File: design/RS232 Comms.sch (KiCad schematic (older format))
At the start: 9 parts, among them J1 JACK_2P, K3 jumper, K4 jumper, U7 MAX232

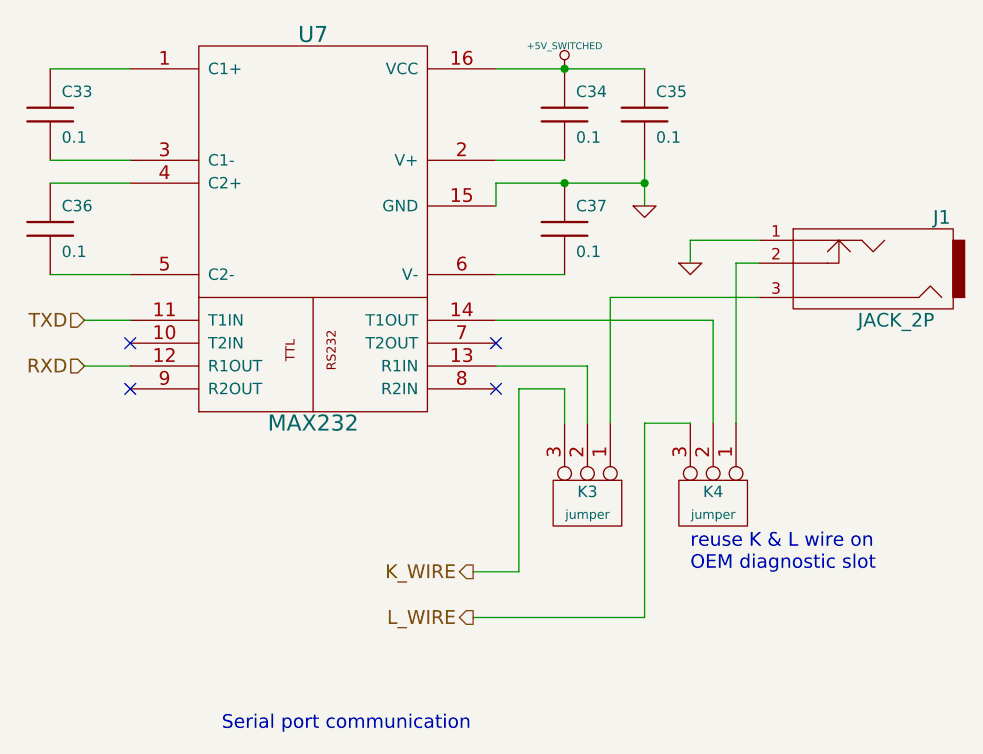
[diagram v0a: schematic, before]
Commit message: revise schema according to Jaguar & Ravage project, eliminate as many errors as possible which were inherited from Puma board. Remove VSS interface, narrow band O2 interface, AC relay output, AC signal input. Make fuel injection configurable which can be batch fired or semi sequential fired
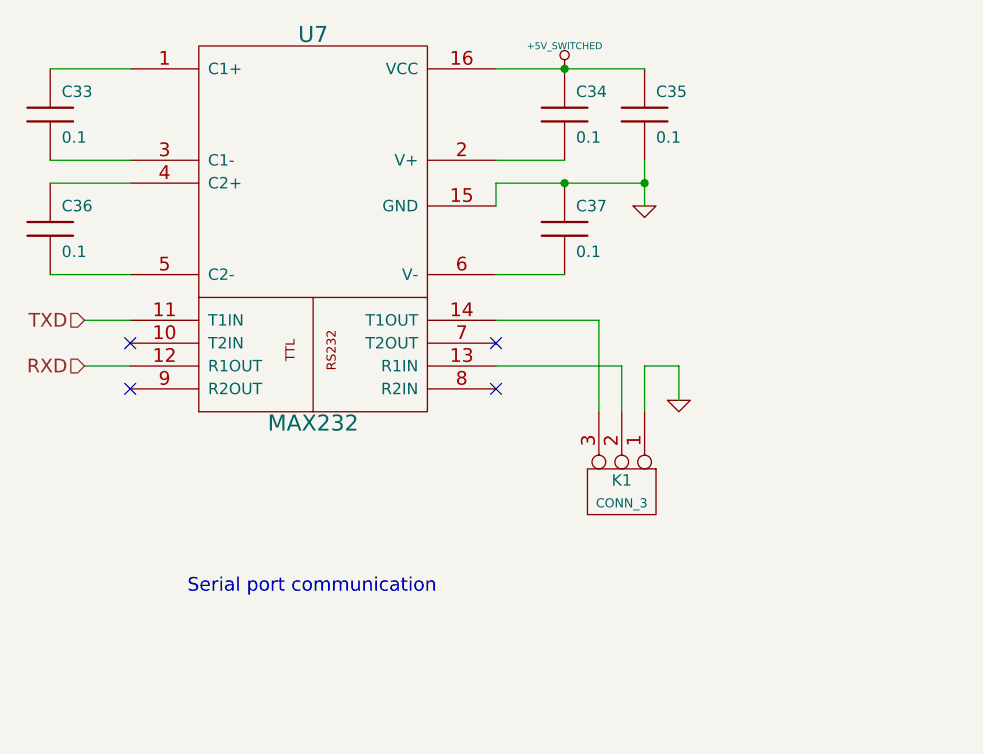
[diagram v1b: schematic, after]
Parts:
- removed J1: JACK_2P, symbol JACK_2P
- removed K3, K4: jumper, symbol CONN_3
- added K1: CONN_3, symbol CONN_3
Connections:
- net GND: now also K1.1 (P1)
- net at U7.14 (T1OUT): now also K1.3 (P3)
- net at U7.13 (R1IN): now also K1.2 (PM)
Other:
- note removed: "reuse K & L wire on\nOEM diagnostic slot"
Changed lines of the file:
@@
-EESchema Schematic File Version 2  date 29/01/2012 19:39:37
+EESchema Schematic File Version 2  date 02/02/2012 00:51:37
 LIBS:power
 LIBS:device
@@
 EELAYER END
 $Descr A4 11700 8267
-Sheet 9 12
+Sheet 8 10
 Title "RS232"
-Date "24 jan 2012"
+Date "1 feb 2012"
 Rev "0.01"
 Comp "diyefi.org"
@@
 Comment4 ""
 $EndDescr
-Connection ~ 6700 3150
 Wire Wire Line
-	6700 3050 6700 3250
+	6850 4100 6850 3950
 Wire Wire Line
-	6900 3500 6900 3400
+	6850 3950 6700 3950
 Wire Wire Line
-	6900 3400 7200 3400
+	6700 3950 6700 4150
 Wire Wire Line
-	7200 3500 7100 3500
+	6500 4150 6500 3750
 Wire Wire Line
-	7100 3500 7100 4200
+	6500 3750 6050 3750
+Connection ~ 6350 2650
 Wire Wire Line
-	6700 4200 6700 5050
+	6050 2650 6700 2650
 Wire Wire Line
-	6700 4200 6900 4200
+	4450 3750 4250 3750
+Connection ~ 6350 3150
 Wire Wire Line
-	6350 4200 6350 4050
+	6350 3550 6050 3550
 Wire Wire Line
-	6350 4050 6150 4050
+	6050 3050 6350 3050
 Wire Wire Line
-	6700 3150 6050 3150
+	4100 3550 4450 3550
+Wire Wire Line
+	4100 2650 4450 2650
+Wire Wire Line
+	4100 3050 4450 3050
+Wire Wire Line
+	4100 3150 4450 3150
+Wire Wire Line
+	6050 3250 6050 3150
 Wire Wire Line
 	4450 3950 4250 3950
 Wire Wire Line
-	6050 3150 6050 3250
+	6050 3150 6700 3150
 Wire Wire Line
-	4100 3150 4450 3150
+	6700 3250 6700 3050
+Connection ~ 6700 3150
 Wire Wire Line
-	4100 3050 4450 3050
+	6050 3950 6600 3950
 Wire Wire Line
-	4100 2650 4450 2650
-Wire Wire Line
-	4100 3550 4450 3550
-Wire Wire Line
-	6050 3050 6350 3050
-Wire Wire Line
-	6350 3550 6050 3550
-Connection ~ 6350 3150
-Wire Wire Line
-	4450 3750 4250 3750
-Wire Wire Line
-	6050 3950 6450 3950
-Wire Wire Line
-	6450 3950 6450 4200
-Wire Wire Line
-	6700 5050 5950 5050
-Wire Wire Line
-	6150 4050 6150 4850
-Wire Wire Line
-	6150 4850 5950 4850
-Wire Wire Line
-	7000 4200 7000 3750
-Wire Wire Line
-	7000 3750 6050 3750
-Wire Wire Line
-	6550 4200 6550 3650
-Wire Wire Line
-	6550 3650 7200 3650
-Wire Wire Line
-	6700 2650 6050 2650
-Connection ~ 6350 2650
+	6600 3950 6600 4150
+$Comp
+L CONN_3 K1
+U 1 1 4F28EFEF
+P 6600 4500
+F 0 "K1" V 6550 4500 50  0000 C CNN
+F 1 "CONN_3" V 6650 4500 40  0000 C CNN
+	1    6600 4500
+	0    1    1    0
+$EndComp
 $Comp
 L C C35
@@
 	1    0    0    -1
 $EndComp
-Text HLabel 5950 5050 0    60   Output ~ 0
-L_WIRE
-Text HLabel 5950 4850 0    60   Output ~ 0
-K_WIRE
 $Comp
-L CONN_3 K3
-U 1 1 4E927716
-P 6450 4550
-F 0 "K3" V 6400 4550 50  0000 C CNN
-F 1 "jumper" V 6500 4550 40  0000 C CNN
-	1    6450 4550
-	0    1    1    0
-$EndComp
-$Comp
-L CONN_3 K4
-U 1 1 4E927715
-P 7000 4550
-F 0 "K4" V 6950 4550 50  0000 C CNN
-F 1 "jumper" V 7050 4550 40  0000 C CNN
-	1    7000 4550
-	0    1    1    0
-$EndComp
-$Comp
-L GND #PWR0104
+L GND #PWR081
 U 1 1 4E92FFAF
-P 6900 3500
-F 0 "#PWR0104" H 6900 3500 30  0001 C CNN
-F 1 "GND" H 6900 3430 30  0001 C CNN
-	1    6900 3500
+P 6850 4100
+F 0 "#PWR081" H 6850 4100 30  0001 C CNN
+F 1 "GND" H 6850 4030 30  0001 C CNN
+	1    6850 4100
 	1    0    0    -1
 $EndComp
 $Comp
-L JACK_2P J1
-U 1 1 4E927849
-P 7650 3500
-F 0 "J1" H 7300 3300 60  0000 C CNN
-F 1 "JACK_2P" H 7500 3750 60  0000 C CNN
-	1    7650 3500
-	-1   0    0    1
-$EndComp
-$Comp
-L +5V_SWITCHED #PWR0105
+L +5V_SWITCHED #PWR082
 U 1 1 4E9277BA
 P 6350 2650
-F 0 "#PWR0105" H 6350 2600 20  0001 C CNN
+F 0 "#PWR082" H 6350 2600 20  0001 C CNN
 F 1 "+5V_SWITCHED" H 6350 2750 30  0000 C CNN
 	1    6350 2650
@@
 NoConn ~ 4450 4050
 NoConn ~ 4450 3850
-Text Notes 4850 5550 0    60   ~ 0
+Text Notes 4700 4950 0    60   ~ 0
 Serial port communication
 $Comp
-L GND #PWR0106
+L GND #PWR083
 U 1 1 4E927717
 P 6700 3250
-F 0 "#PWR0106" H 6700 3250 30  0001 C CNN
+F 0 "#PWR083" H 6700 3250 30  0001 C CNN
 F 1 "GND" H 6700 3180 30  0001 C CNN
 	1    6700 3250
 	1    0    0    -1
 $EndComp
-Text Notes 6900 4850 0    60   ~ 0
-reuse K & L wire on\nOEM diagnostic slot
 $EndSCHEMATC

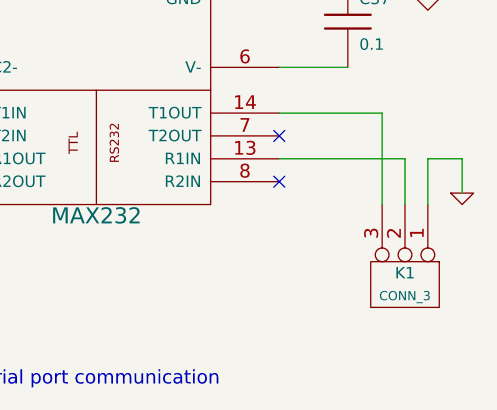
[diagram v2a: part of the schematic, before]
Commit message: make new footprint for screw connector, redesign ignition gnd & all lowside gnd
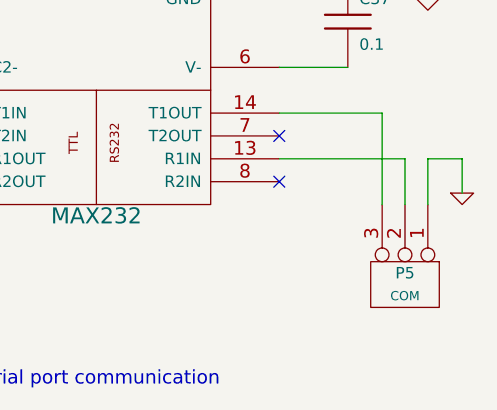
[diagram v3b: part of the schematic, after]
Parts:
- P5: renamed from K1; value CONN_3 -> COM
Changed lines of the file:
@@
-EESchema Schematic File Version 2  date 02/02/2012 10:58:16
+EESchema Schematic File Version 2  date 07/02/2012 00:44:28
 LIBS:power
 LIBS:device
@@
 Sheet 8 10
 Title "RS232"
-Date "2 feb 2012"
+Date "6 feb 2012"
 Rev "0.01"
 Comp "diyefi.org"
@@
 	6600 3950 6600 4150
 $Comp
-L CONN_3 K1
+L CONN_3 P5
 U 1 1 4F28EFEF
 P 6600 4500
-F 0 "K1" V 6550 4500 50  0000 C CNN
-F 1 "CONN_3" V 6650 4500 40  0000 C CNN
+F 0 "P5" V 6550 4500 50  0000 C CNN
+F 1 "COM" V 6650 4500 40  0000 C CNN
 	1    6600 4500
 	0    1    1    0
@@
 $EndComp
 $Comp
-L GND #PWR081
+L GND #PWR084
 U 1 1 4E92FFAF
 P 6850 4100
-F 0 "#PWR081" H 6850 4100 30  0001 C CNN
+F 0 "#PWR084" H 6850 4100 30  0001 C CNN
 F 1 "GND" H 6850 4030 30  0001 C CNN
 	1    6850 4100
@@
 $EndComp
 $Comp
-L +5V_SWITCHED #PWR082
+L +5V_SWITCHED #PWR085
 U 1 1 4E9277BA
 P 6350 2650
-F 0 "#PWR082" H 6350 2600 20  0001 C CNN
+F 0 "#PWR085" H 6350 2600 20  0001 C CNN
 F 1 "+5V_SWITCHED" H 6350 2750 30  0000 C CNN
 	1    6350 2650
@@
 Serial port communication
 $Comp
-L GND #PWR083
+L GND #PWR086
 U 1 1 4E927717
 P 6700 3250
-F 0 "#PWR083" H 6700 3250 30  0001 C CNN
+F 0 "#PWR086" H 6700 3250 30  0001 C CNN
 F 1 "GND" H 6700 3180 30  0001 C CNN
 	1    6700 3250
